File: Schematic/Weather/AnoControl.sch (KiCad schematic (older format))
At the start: 0 parts

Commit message: More Board Data
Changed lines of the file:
@@
 EESchema Schematic File Version 4
+LIBS:Weather-cache
 EELAYER 29 0
 EELAYER END
 $Descr A4 11693 8268
 encoding utf-8
-Sheet 6 7
+Sheet 6 10
 Title ""
 Date ""
@@
 Text HLabel 2500 2400 0    50   Input ~ 0
 J6_P3
+Text HLabel 8000 2000 0    50   Input ~ 0
+J7_P1
+Text HLabel 8000 2200 0    50   Input ~ 0
+J7_P2
+Text HLabel 8000 2400 0    50   Input ~ 0
+J7_P3
+Text HLabel 8000 2600 0    50   Input ~ 0
+J7_P4
+Text HLabel 2850 3600 0    50   Input ~ 0
+J13_P1
+Text HLabel 2850 3800 0    50   Input ~ 0
+J13_P2
+Text HLabel 2850 4000 0    50   Input ~ 0
+J13_P3
+Text HLabel 2850 4200 0    50   Input ~ 0
+J13_P4
+Text HLabel 2850 4400 0    50   Input ~ 0
+J13_P5
+Text HLabel 2850 4600 0    50   Input ~ 0
+J13_P6
+Text HLabel 2850 4800 0    50   Input ~ 0
+J13_P7
+Text HLabel 2850 5000 0    50   Input ~ 0
+J13_P8
 $EndSCHEMATC

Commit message: update before south board added
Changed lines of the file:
@@
 Text HLabel 2850 4400 0    50   Input ~ 0
 J13_P5
-Text HLabel 2850 4600 0    50   Input ~ 0
-J13_P6
-Text HLabel 2850 4800 0    50   Input ~ 0
-J13_P7
-Text HLabel 2850 5000 0    50   Input ~ 0
-J13_P8
 $EndSCHEMATC

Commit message: more board layouts
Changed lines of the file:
@@
 $Descr A4 11693 8268
 encoding utf-8
-Sheet 6 10
+Sheet 6 11
 Title ""
 Date ""
@@
 Text HLabel 2850 4400 0    50   Input ~ 0
 J13_P5
+Text HLabel 2850 4950 0    50   Input ~ 0
+J14_P1
+Text HLabel 2850 5150 0    50   Input ~ 0
+J14_P2
+Text HLabel 2850 5350 0    50   Input ~ 0
+J14_P3
+Text HLabel 2850 5550 0    50   Input ~ 0
+J14_P4
+Text HLabel 2850 5750 0    50   Input ~ 0
+J14_P5
 $EndSCHEMATC

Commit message: More boards added
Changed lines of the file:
@@
 $Descr A4 11693 8268
 encoding utf-8
-Sheet 6 11
+Sheet 11 13
 Title ""
 Date ""
@@
 Text HLabel 2850 5750 0    50   Input ~ 0
 J14_P5
+Text HLabel 8000 3450 0    50   Input ~ 0
+J21_P1
+Text HLabel 8000 3600 0    50   Input ~ 0
+J21_P2
+Text HLabel 8000 3750 0    50   Input ~ 0
+J21_P3
+Text HLabel 8000 3900 0    50   Input ~ 0
+J21_P4
+Text HLabel 8000 4050 0    50   Input ~ 0
+J21_P5
+Text HLabel 8000 4500 0    50   Input ~ 0
+J22_P1
+Text HLabel 8000 4650 0    50   Input ~ 0
+J22_P2
+Text HLabel 8000 4800 0    50   Input ~ 0
+J22_P3
+Text HLabel 8000 4950 0    50   Input ~ 0
+J22_P4
+Text HLabel 8000 5100 0    50   Input ~ 0
+J22_P5
 $EndSCHEMATC

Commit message: more changes
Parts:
- added J13: 3_Way_Wire, Connector_PinHeader_2.54mm:PinHeader_1x03_P2.54mm_Vertical, symbol MyComponents:3_Way_Wire
- added J14, J15, J16, J18: 5_Way_Wire, Connector_PinHeader_2.54mm:PinHeader_1x05_P2.54mm_Vertical, symbol MyComponents:5_Way_Wire
- added J17: 4_Way_Wire, Connector_PinHeader_2.54mm:PinHeader_1x04_P2.54mm_Vertical, symbol MyComponents:4_Way_Wire
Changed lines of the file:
@@
 $Descr A4 11693 8268
 encoding utf-8
-Sheet 11 14
+Sheet 11 15
 Title ""
 Date ""
@@
 Text HLabel 8000 5100 0    50   Input ~ 0
 J22_P5
+$Comp
+L MyComponents:4_Way_Wire J17
+U 1 1 5CB50F85
+P 6150 1650
+F 0 "J17" H 6319 1411 50  0000 L CNN
+F 1 "4_Way_Wire" H 6319 1320 50  0000 L CNN
+F 2 "Connector_PinHeader_2.54mm:PinHeader_1x04_P2.54mm_Vertical" H 6050 1700 50  0001 C CNN
+F 3 "" H 6050 1700 50  0001 C CNN
+	1    6150 1650
+	1    0    0    -1
+$EndComp
+$Comp
+L MyComponents:3_Way_Wire J13
+U 1 1 5CB53FC1
+P 3500 2100
+F 0 "J13" H 3669 2061 50  0000 L CNN
+F 1 "3_Way_Wire" H 3669 1970 50  0000 L CNN
+F 2 "Connector_PinHeader_2.54mm:PinHeader_1x03_P2.54mm_Vertical" H 3500 2100 50  0001 C CNN
+F 3 "" H 3500 2100 50  0001 C CNN
+	1    3500 2100
+	1    0    0    -1
+$EndComp
+$Comp
+L MyComponents:5_Way_Wire J14
+U 1 1 5CB547B3
+P 4150 3750
+F 0 "J14" H 4319 3611 50  0000 L CNN
+F 1 "5_Way_Wire" H 4319 3520 50  0000 L CNN
+F 2 "Connector_PinHeader_2.54mm:PinHeader_1x05_P2.54mm_Vertical" H 4150 3750 50  0001 C CNN
+F 3 "" H 4150 3750 50  0001 C CNN
+	1    4150 3750
+	1    0    0    -1
+$EndComp
+$Comp
+L MyComponents:5_Way_Wire J15
+U 1 1 5CB550C8
+P 4150 5100
+F 0 "J15" H 4319 4961 50  0000 L CNN
+F 1 "5_Way_Wire" H 4319 4870 50  0000 L CNN
+F 2 "Connector_PinHeader_2.54mm:PinHeader_1x05_P2.54mm_Vertical" H 4150 5100 50  0001 C CNN
+F 3 "" H 4150 5100 50  0001 C CNN
+	1    4150 5100
+	1    0    0    -1
+$EndComp
+$Comp
+L MyComponents:5_Way_Wire J16
+U 1 1 5CB55866
+P 6100 4050
+F 0 "J16" H 6113 3455 50  0000 C CNN
+F 1 "5_Way_Wire" H 6113 3546 50  0000 C CNN
+F 2 "Connector_PinHeader_2.54mm:PinHeader_1x05_P2.54mm_Vertical" H 6100 4050 50  0001 C CNN
+F 3 "" H 6100 4050 50  0001 C CNN
+	1    6100 4050
+	-1   0    0    1
+$EndComp
+$Comp
+L MyComponents:5_Way_Wire J18
+U 1 1 5CB5681F
+P 6250 5200
+F 0 "J18" H 6263 4605 50  0000 C CNN
+F 1 "5_Way_Wire" H 6263 4696 50  0000 C CNN
+F 2 "Connector_PinHeader_2.54mm:PinHeader_1x05_P2.54mm_Vertical" H 6250 5200 50  0001 C CNN
+F 3 "" H 6250 5200 50  0001 C CNN
+	1    6250 5200
+	-1   0    0    1
+$EndComp
 $EndSCHEMATC

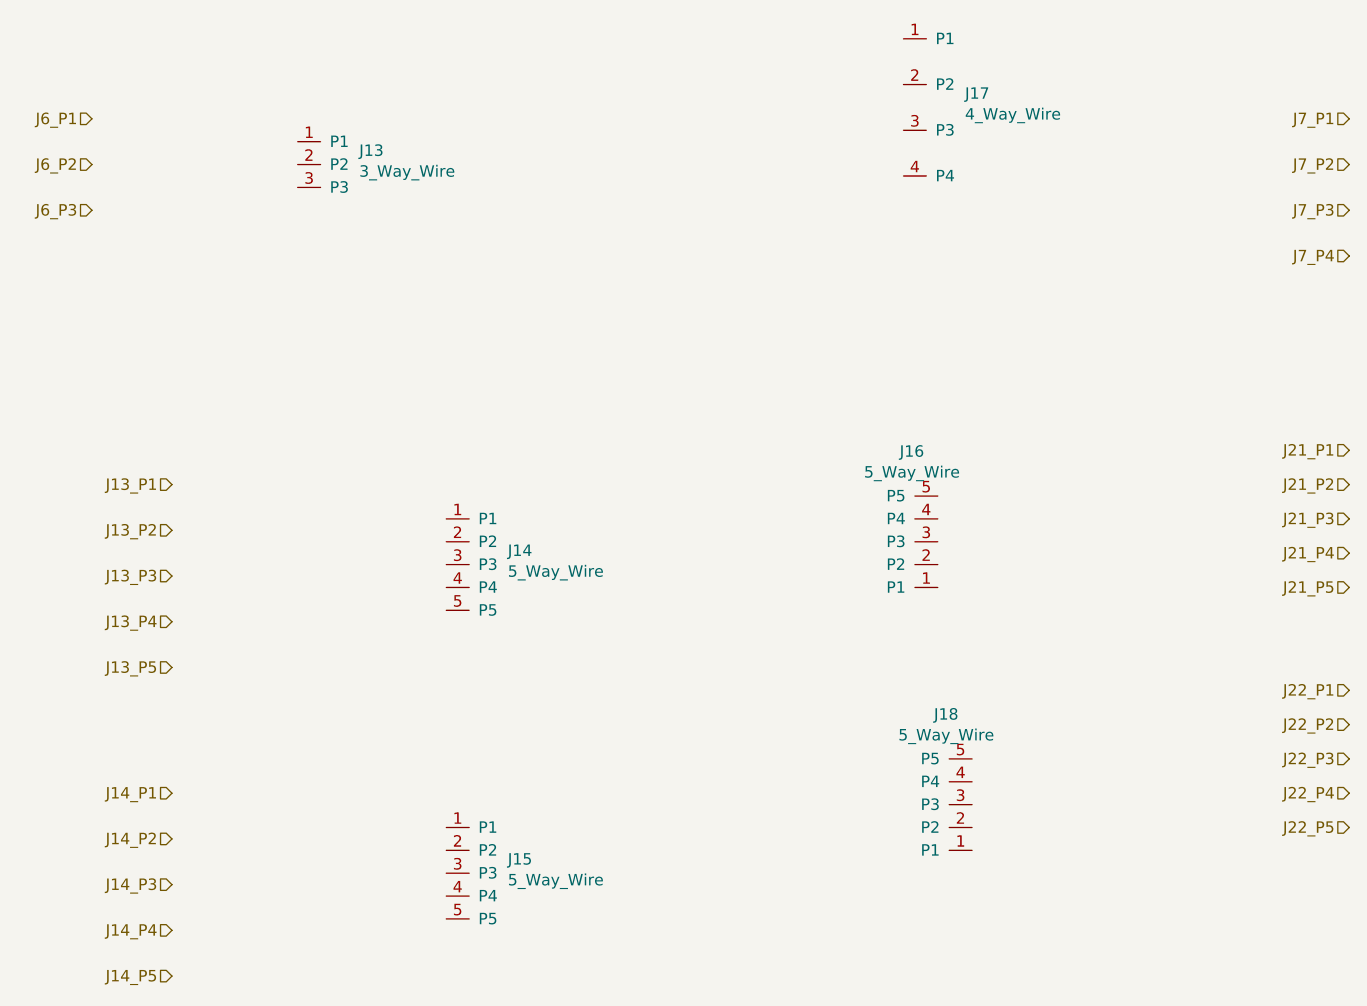
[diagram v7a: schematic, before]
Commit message: Connector relable start
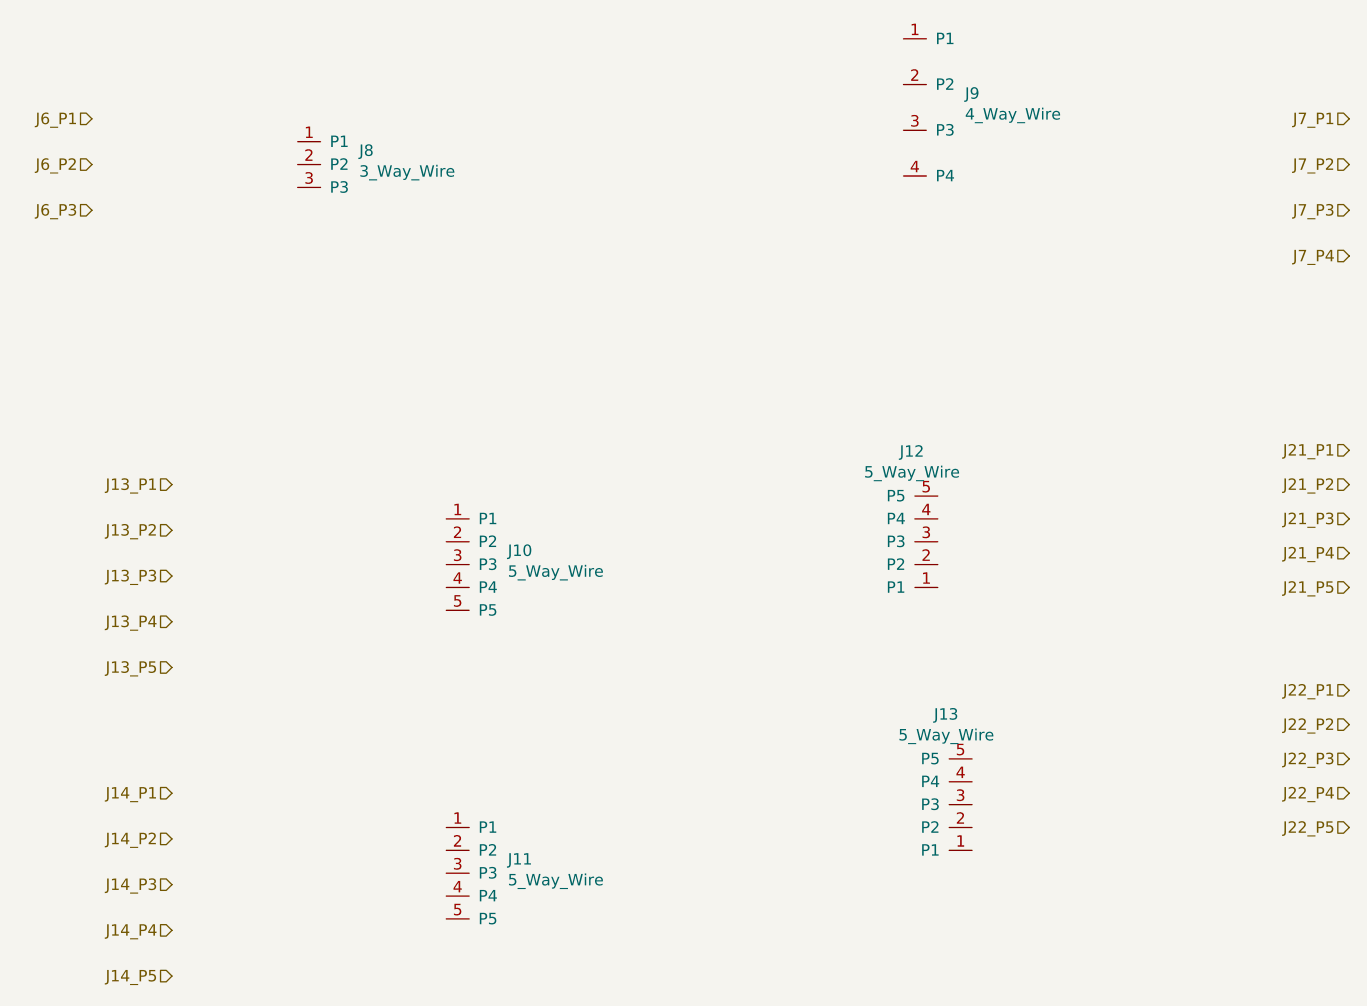
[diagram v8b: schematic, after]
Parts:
- renumbered J14 to J10, J15 to J11, J16 to J12, J18 to J13, J13 to J8, J17 to J9
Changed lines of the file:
@@
 $Descr A4 11693 8268
 encoding utf-8
-Sheet 11 15
+Sheet 15 15
 Title ""
 Date ""
@@
 J22_P5
 $Comp
-L MyComponents:4_Way_Wire J17
+L MyComponents:4_Way_Wire J9
 U 1 1 5CB50F85
 P 6150 1650
-F 0 "J17" H 6319 1411 50  0000 L CNN
+F 0 "J9" H 6319 1411 50  0000 L CNN
 F 1 "4_Way_Wire" H 6319 1320 50  0000 L CNN
 F 2 "Connector_PinHeader_2.54mm:PinHeader_1x04_P2.54mm_Vertical" H 6050 1700 50  0001 C CNN
@@
 $EndComp
 $Comp
-L MyComponents:3_Way_Wire J13
+L MyComponents:3_Way_Wire J8
 U 1 1 5CB53FC1
 P 3500 2100
-F 0 "J13" H 3669 2061 50  0000 L CNN
+F 0 "J8" H 3669 2061 50  0000 L CNN
 F 1 "3_Way_Wire" H 3669 1970 50  0000 L CNN
 F 2 "Connector_PinHeader_2.54mm:PinHeader_1x03_P2.54mm_Vertical" H 3500 2100 50  0001 C CNN
@@
 $EndComp
 $Comp
-L MyComponents:5_Way_Wire J14
+L MyComponents:5_Way_Wire J10
 U 1 1 5CB547B3
 P 4150 3750
-F 0 "J14" H 4319 3611 50  0000 L CNN
+F 0 "J10" H 4319 3611 50  0000 L CNN
 F 1 "5_Way_Wire" H 4319 3520 50  0000 L CNN
 F 2 "Connector_PinHeader_2.54mm:PinHeader_1x05_P2.54mm_Vertical" H 4150 3750 50  0001 C CNN
@@
 $EndComp
 $Comp
-L MyComponents:5_Way_Wire J15
+L MyComponents:5_Way_Wire J11
 U 1 1 5CB550C8
 P 4150 5100
-F 0 "J15" H 4319 4961 50  0000 L CNN
+F 0 "J11" H 4319 4961 50  0000 L CNN
 F 1 "5_Way_Wire" H 4319 4870 50  0000 L CNN
 F 2 "Connector_PinHeader_2.54mm:PinHeader_1x05_P2.54mm_Vertical" H 4150 5100 50  0001 C CNN
@@
 $EndComp
 $Comp
-L MyComponents:5_Way_Wire J16
+L MyComponents:5_Way_Wire J12
 U 1 1 5CB55866
 P 6100 4050
-F 0 "J16" H 6113 3455 50  0000 C CNN
+F 0 "J12" H 6113 3455 50  0000 C CNN
 F 1 "5_Way_Wire" H 6113 3546 50  0000 C CNN
 F 2 "Connector_PinHeader_2.54mm:PinHeader_1x05_P2.54mm_Vertical" H 6100 4050 50  0001 C CNN
@@
 $EndComp
 $Comp
-L MyComponents:5_Way_Wire J18
+L MyComponents:5_Way_Wire J13
 U 1 1 5CB5681F
 P 6250 5200
-F 0 "J18" H 6263 4605 50  0000 C CNN
+F 0 "J13" H 6263 4605 50  0000 C CNN
 F 1 "5_Way_Wire" H 6263 4696 50  0000 C CNN
 F 2 "Connector_PinHeader_2.54mm:PinHeader_1x05_P2.54mm_Vertical" H 6250 5200 50  0001 C CNN
